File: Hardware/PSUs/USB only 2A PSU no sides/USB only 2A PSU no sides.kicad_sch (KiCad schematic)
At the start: 3 parts

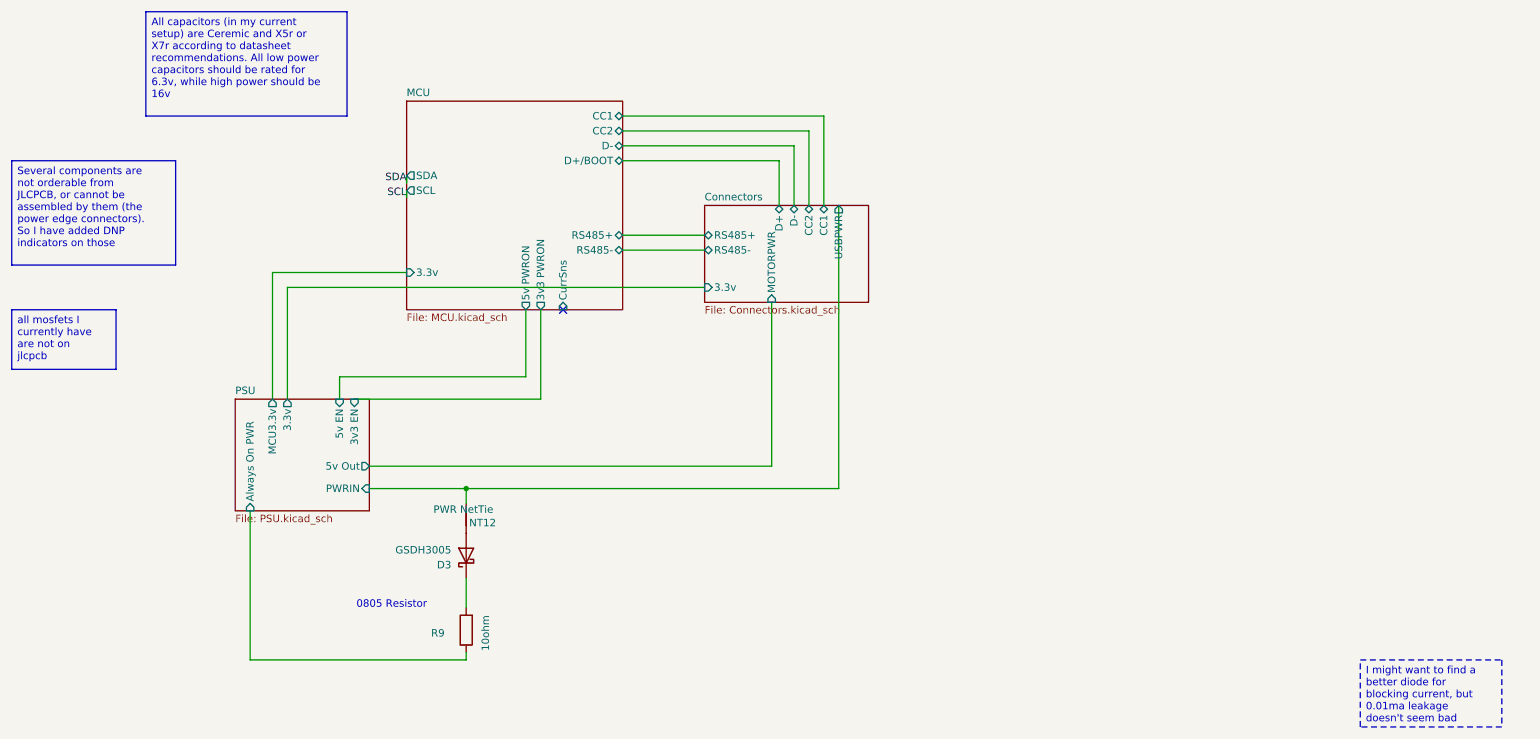
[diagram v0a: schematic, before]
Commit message: Finished schematic, started arrangement
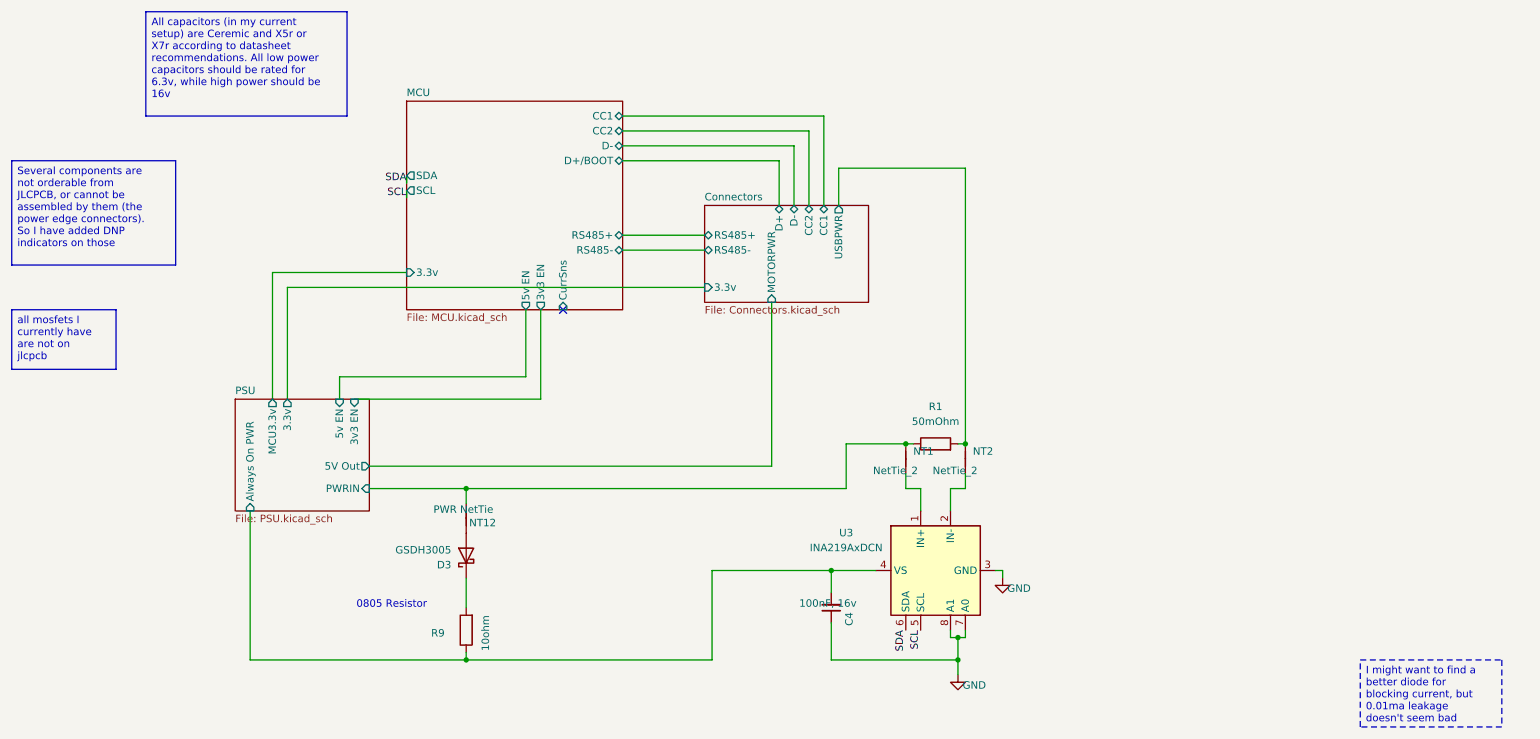
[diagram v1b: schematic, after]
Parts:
- added C4: 100nF, 16v, Capacitor_SMD:C_0603_1608Metric, symbol Device:C_Small
- added NT1, NT2: NetTie_2, custom_Connector:NetTie-2_SMD_Pad0.2mm, symbol Device:NetTie_2
- added R1: 50mOhm, Resistor_SMD:R_2512_6332Metric, symbol Device:R
- added U3: INA219AxDCN, Package_TO_SOT_SMD:SOT-23-8, symbol Sensor_Energy:INA219AxDCN
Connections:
- net Connectors/USBPWR: now also NT2.2, R1.2; no longer NT12.2
- net PSU/Always On PWR: now also C4.2, U3.4 (VS)
- net SCL: now also U3.5 (SCL)
- net SDA: now also U3.6 (SDA)
- new net: NT1.1, U3.1 (IN+)
- new net: NT2.1, U3.2 (IN-)
- new net GND: C4.1, U3.3 (GND), U3.7 (A0), U3.8 (A1)
- new net PSU/PWRIN: NT1.2, NT12.2, R1.1
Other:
- sheet MCU ports: added 3v3 EN, 5v EN; removed 3v3 PWRON, 5v PWRON
- sheet PSU ports: added 5V Out; removed 5v Out

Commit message: Moved current sense to PSU schematic
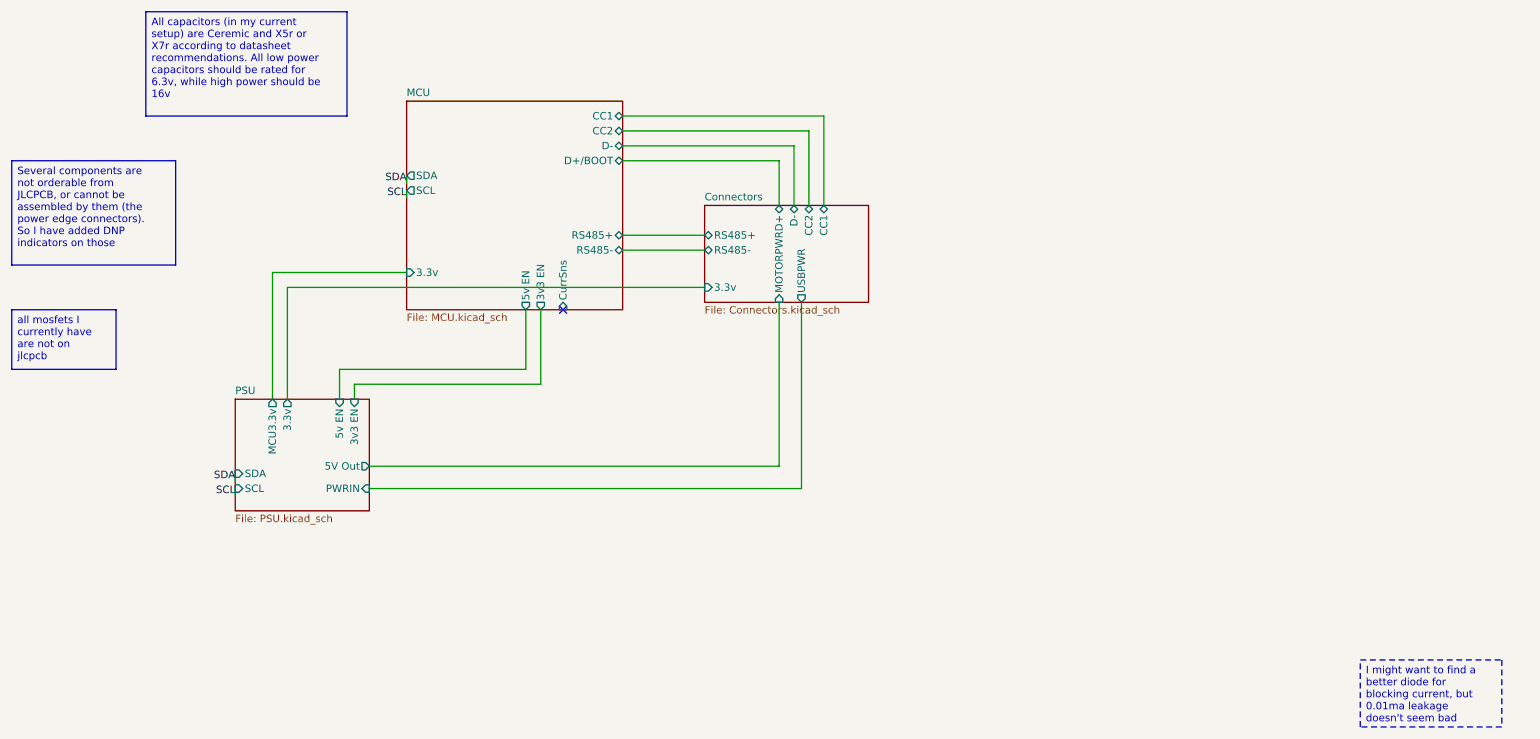
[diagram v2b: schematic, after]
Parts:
- removed C4: 100nF, 16v, Capacitor_SMD:C_0603_1608Metric, symbol Device:C_Small
- removed D3: GSDH3005, Diode_SMD:D_0402_1005Metric, symbol Device:D_Schottky
- removed NT1, NT2: NetTie_2, custom_Connector:NetTie-2_SMD_Pad0.2mm, symbol Device:NetTie_2
- removed NT12: PWR NetTie, custom_Connector:NetTie-2_SMD_Pad0.28mm, symbol Device:NetTie_2
- removed R1: 50mOhm, Resistor_SMD:R_2512_6332Metric, symbol Device:R
- removed R9: 10ohm, Resistor_SMD:R_0805_2012Metric, symbol Device:R
- removed U3: INA219AxDCN, Package_TO_SOT_SMD:SOT-23-8, symbol Sensor_Energy:INA219AxDCN
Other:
- sheet PSU ports: added SCL, SDA; removed Always On PWR
- note removed: "0805 Resistor"
